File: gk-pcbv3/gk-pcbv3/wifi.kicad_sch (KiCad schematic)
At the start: 8 parts, among them J16 Conn_01x05, U25 ATWILC3000-MR110CA

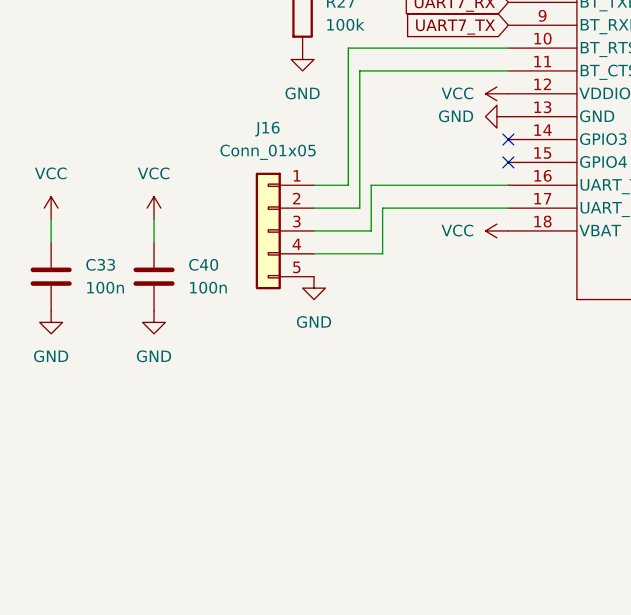
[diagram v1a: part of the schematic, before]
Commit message: update schematics for new vreg design
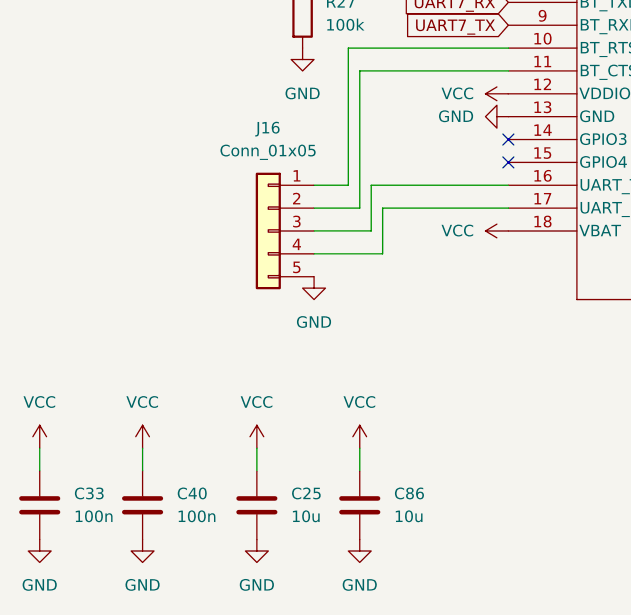
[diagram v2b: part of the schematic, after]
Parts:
- added C25, C86: 10u, Capacitor_SMD:C_0805_2012Metric, symbol Device:C
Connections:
- net GND: now also C25.2, C86.2
- net VCC: now also C25.1, C86.1
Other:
- moved on the sheet: C33, C40
